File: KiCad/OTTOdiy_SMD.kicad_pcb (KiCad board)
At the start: 4 copper layers, 297 x 91 mm, 421 parts, among them CN201 1x4 MALE Molex PicoBlade, CN202 1x4 MALE Molex PicoBlade, J1 Conn_ARM_JTAG_SWD_10, J2 Conn_02x04, J201 Raspberry Pi Connector, J202 Conn_02x04, J203 Conn_02x05, J204 Conn_02x05, J205 Conn_02x04, J206 Conn_02x06, J207 Conn_02x03, Q1 AO4485, SW1 ALPS SKHH OR SKPF, SW10 ALPS SKHH OR SKPF, SW11 ALPS SKHH OR SKPF, SW12 ALPS SKHH OR SKPF, SW13 ALPS SKHH OR SKPF, SW14 ALPS SKHH OR SKPF, SW15 ALPS SKHH OR SKPF, SW16 ALPS SKHH OR SKPF, SW17 ALPS SKHH OR SKPF, SW18 ALPS SKHH OR SKPF, SW19 ALPS SKHH OR SKPF, SW2 ALPS SKHH OR SKPF, SW20 ALPS SKHH OR SKPF, SW201 6x6x5mm, SW202 SW_DIP_x02, SW203 6x6x5.85mm (RA), SW21 ALPS SKHH OR SKPF, SW22 ALPS SKHH OR SKPF, SW23 ALPS SKHH OR SKPF, SW24 ALPS SKHH OR SKPF, SW25 ALPS SKHH OR SKPF, SW26 ALPS SKHH OR SKPF, SW27 6x6x13mm, SW28 6x6x13mm, SW29 6x6x13mm, SW3 ALPS SKHH OR SKPF, SW30 6x6x13mm, SW31 6x6x13mm, SW32 6x6x13mm, SW33 6x6x13mm, SW34 6x6x13mm, SW35 6x6x13mm, SW36 6x6x13mm, SW37 6x6x13mm, SW38 6x6x13mm, SW39 6x6x13mm, SW4 ALPS SKHH OR SKPF, SW40 6x6x13mm, SW41 6x6x13mm, SW42 6x6x13mm, SW43 6x6x13mm, SW44 6x6x13mm, SW45 6x6x13mm, SW46 6x6x13mm, SW47 6x6x13mm, SW48 SW_DIP_x02, SW49 SW_SP3T (DP3T Parallel), SW5 ALPS SKHH OR SKPF, SW6 ALPS SKHH OR SKPF, SW7 ALPS SKHH OR SKPF, SW8 ALPS SKHH OR SKPF, SW9 ALPS SKHH OR SKPF, U1 SN74LV1T125_SOT-23_A, U2 TPS22918_SOT23-6_A, U202 STM32F407VGTx, U204 USB6B1, U205 SN74HC14, U206 H11L1S, U207 WM8731, U208 TPS79533, U3 LTC3112_TSSOP20_A, U4 TLV62568_SOT-23-5_A, U5 TPS22918_SOT23-6_A, Y201 8MHz, Y202 32.768kHz, Y203 12.288MHz

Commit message: more power supply routing and stm32 placement
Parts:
- moved C222 90.1 mm to (62.9, 52.5)
- moved C226 90.1 mm to (58.9, 58.5)
- moved C53 90.1 mm to (62.9, 49.5)
- moved C58 90.1 mm to (62.9, 46.5)
- moved C68 90.1 mm to (89.9, 36.3)
- moved R203 90.1 mm to (90.9, 45.0)
- moved R206 90.1 mm to (62.9, 55.5)
- moved R207 90.1 mm to (62.9, 58.5)
- moved SW202 90.1 mm to (83.6, 45.0)
- moved U206 90.1 mm to (83.6, 36.3)
- moved C211 84.2 mm to (56.6, 87.1)
- moved C221 84.2 mm to (56.6, 82.1)
- moved C50 84.2 mm to (53.6, 82.1)
- moved C54 84.2 mm to (65.6, 82.1)
- moved R204 84.2 mm to (59.6, 82.1)
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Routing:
- net GND: track 66.2 -> 231.8 mm, vias 37 -> 38
- net +3V3_MCU: track 35.5 -> 3.02 mm
- net +3V3A_MCU: track 17.1 -> 0.00 mm
- net /MCU/USBD_N: track 20.8 -> 6.91 mm
- net /MCU/USBD_P: track 20.1 -> 6.73 mm
- net /MCU/OSC_OUT: track 27.5 -> 14.2 mm, vias 0 -> 1
- net /MCU/OSC_IN: track 23.3 -> 14.3 mm, vias 0 -> 1
- net Net-(D9-Pad2): track 0.00 -> 8.30 mm
- net Net-(D8-Pad2): track 0.00 -> 8.30 mm
- net Net-(D7-Pad2): track 0.00 -> 8.30 mm
- net Net-(D6-Pad2): track 0.00 -> 8.30 mm
- net Net-(D23-Pad2): track 0.00 -> 8.30 mm
- net Net-(D22-Pad2): track 0.00 -> 8.30 mm
- net Net-(D21-Pad2): track 0.00 -> 8.30 mm
- net Net-(D20-Pad2): track 0.00 -> 8.30 mm
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- added copper zone on B.Cu, net +5V_LEDS

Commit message: routed mcu decoupling
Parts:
- removed C223: 1uF, Capacitor_SMD:C_0805_2012Metric_Pad1.15x1.40mm_HandSolder
- removed C56: 100nF, Capacitor_SMD:C_0805_2012Metric_Pad1.15x1.40mm_HandSolder
- BT201: moved to F.Cu
- C96, C97, FB1: moved to B.Cu
- moved FB1 108.9 mm to (105.0, 158.3), turned to 180 degrees
- moved BT201 99.9 mm to (110.5, 129.0)
- moved C96 98.4 mm to (105.0, 143.1)
- moved C53 96.1 mm to (81.0, 143.9)
- moved C97 93.8 mm to (105.0, 145.0)
- moved C51 90.6 mm to (98.0, 162.1), turned to 270 degrees
- moved C50 87.3 mm to (105.0, 152.6), turned to 0 degrees
- moved C52 84.9 mm to (87.0, 162.1), turned to 270 degrees
- moved C49 84.7 mm to (105.0, 146.9)
- moved C218 76.9 mm to (105.0, 141.2)
- moved C55 75.4 mm to (105.0, 154.5)
- moved C219 74.4 mm to (105.0, 156.4)
- moved C211 67.4 mm to (100.9, 137.9), turned to 90 degrees
- moved C54 65.0 mm to (99.0, 137.9), turned to 90 degrees
- moved C205 24.0 mm to (105.0, 150.7)
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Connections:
- Y202 pad 1: /MCU/OSC32_OUT -> /MCU/OSC32_IN
- Y202 pad 2: /MCU/OSC32_IN -> GND
- Y202 pad 3: (no net) -> GND
- Y202 pad 4: (no net) -> /MCU/OSC32_OUT
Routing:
- net Net-(LED18-Pad1): track 0.00 -> 37.7 mm
- net GND: track 231.8 -> 257.6 mm, vias 38 -> 52
- net +3V3_MCU: track 3.02 -> 28.6 mm, vias 5 -> 12
- net /MCU/VBAT: track 0.00 -> 21.3 mm, vias 0 -> 1
- net Net-(LED19-Pad1): track 0.00 -> 14.2 mm
- net Net-(LED17-Pad1): track 0.00 -> 14.2 mm
- net +3V3A_MCU: track 0.00 -> 10.1 mm
- net /MCU/OSC32_IN: track 2.25 -> 12.2 mm
- net /MCU/OSC32_OUT: track 2.25 -> 10.8 mm
- net Net-(LED21-Pad1): track 42.9 -> 38.0 mm
- net Net-(LED23-Pad1): track 36.1 -> 32.2 mm
- net +5V_LEDS: track 167.5 -> 169.5 mm, vias 6 -> 5
- net Net-(LED4-Pad1): track 20.5 -> 18.8 mm
- net /MCU/OSC_OUT: track 14.2 -> 15.3 mm
- net /MCU/OSC_IN: track 14.3 -> 15.3 mm
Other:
- net class Default: clearance 0.254 -> 0.2032
- rule trace_clearance: 0.254 -> 0.2032

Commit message: fix peripheral connections and route more critical components
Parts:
- added C56: 100nF, Capacitor_SMD:C_0805_2012Metric_Pad1.15x1.40mm_HandSolder, B.Cu at (105.0, 162.1)
- added R29: 10k, Resistor_SMD:R_0805_2012Metric_Pad1.15x1.40mm_HandSolder, B.Cu at (105.0, 164.0)
- added R30: 10k, Resistor_SMD:R_0805_2012Metric_Pad1.15x1.40mm_HandSolder, B.Cu at (105.0, 165.9)
- added TP1: TestPoint, TestPoint:TestPoint_Keystone_5000-5004_Miniature, F.Cu at (181.4, 83.8)
- C57, R5, R8: moved to B.Cu
- PHOTO201: value ALS-PDIC243-3B -> VAL**
- USB201: value USB_B -> VAL**
- moved R28 205.1 mm to (81.0, 151.9), turned to 180 degrees
- moved D57 201.1 mm to (81.0, 153.8), turned to 180 degrees
- moved R5 138.2 mm to (61.1, 134.7), turned to 90 degrees
- moved R8 131.6 mm to (59.2, 134.7), turned to 90 degrees
- moved C57 102.2 mm to (105.0, 160.2), turned to 180 degrees
- moved R206 94.3 mm to (81.0, 148.1)
- moved R207 93.2 mm to (81.0, 150.0)
- moved C222 93.0 mm to (81.9, 143.6), turned to 90 degrees
- moved C221 85.7 mm to (87.5, 162.1)
- moved J1 42.3 mm to (103.0, 122.6)
- moved C53 3.70 mm to (82.8, 140.8)
- moved BT201 1.60 mm to (112.1, 129.0)
- moved U204 1.50 mm to (79.5, 125.0)
- moved C52 1.45 mm to (85.5, 162.1)
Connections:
- net /MCU/PERIPHERALS/USBD_N_CON renamed /MCU/PERIPHERALS/USBCON_N
- net /MCU/PERIPHERALS/USBD_P_CON renamed /MCU/PERIPHERALS/USBCON_P
- R28 pad 1: Net-(R28-Pad1) -> /MCU/STATUS_LED
- SW48 pad 1: +5V_REG -> +3V3_MCU
- SW48 pad 2: +5V_REG -> +3V3_MCU
- U202 pad 16: /MCU/DC_IN_DIV_5 -> (no net)
- U202 pad 17: /MCU/5V_REG_IOUT -> (no net)
- U202 pad 18: /MCU/BRIGHTNESS -> (no net)
- U202 pad 23: PWR_BUTTON -> /MCU/DC_IN_DIV_5
- U202 pad 24: (no net) -> /MCU/BRIGHTNESS
- U202 pad 25: (no net) -> /MCU/3V3_RASPI_DIV_2
- U202 pad 26: (no net) -> /MCU/5V_REG_IOUT
- U202 pad 33: /MCU/GATE_IO_1 -> /MCU/EXP_GPIO_1_ADC
- U202 pad 34: /MCU/GATE_IO_2 -> /MCU/EXP_GPIO_2_ADC
- U202 pad 35: /MCU/EXP_GPIO_1_ADC -> /MCU/GATE_IO_1
- U202 pad 36: /MCU/EXP_GPIO_2_ADC -> /MCU/GATE_IO_2
- U202 pad 38: /MCU/EXP_GPIO_3_PWM -> (no net)
- U202 pad 39: /MCU/EXP_GPIO_4_PWM -> (no net)
- U202 pad 40: /MCU/EXP_GPIO_5_PWM -> /MCU/EXP_GPIO_3_PWM
- U202 pad 41: /MCU/EXP_GPIO_6_PWM -> (no net)
- U202 pad 42: (no net) -> /MCU/EXP_GPIO_4_PWM
- U202 pad 44: Net-(R28-Pad1) -> /MCU/EXP_GPIO_5_PWM
- U202 pad 45: /MCU/5V_PWM_SYNC -> /MCU/EXP_GPIO_6_PWM
- U202 pad 62: (no net) -> /PWM1_GPIO13_RASPI
- U202 pad 63: /GPIO0_RASPI -> /MCU/STATUS_LED
- U202 pad 64: /GPIO1_RASPI -> /MCU/5V_PWM_SYNC
- U202 pad 65: /PWM1_GPIO13_RASPI -> /MCU/MCU_PC8
- U202 pad 81: Net-(R25-Pad1) -> PWR_BUTTON
- U202 pad 82: (no net) -> Net-(R25-Pad1)
- U202 pad 92: (no net) -> /GPIO0_RASPI
- U202 pad 93: (no net) -> /GPIO1_RASPI
- U202 pad 97: (no net) -> /MCU/LED_PWR_EN
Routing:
- net /MCU/+5V_USB: track 55.8 -> 81.9 mm, vias 0 -> 2
- net /MCU/USBD_N: track 6.91 -> 24.3 mm
- net /MCU/USBD_P: track 6.73 -> 23.5 mm
- net /MCU/DC_IN: track 27.7 -> 38.5 mm, vias 8 -> 9
- net /MCU/DC_IN_DIV_5: track 0.00 -> 9.75 mm
- net GND: track 257.6 -> 266.7 mm, vias 52 -> 53
- net +3V3_MCU: track 28.6 -> 32.8 mm
- net /MCU/I2C2_SDA: track 0.00 -> 3.97 mm
- net /MCU/3V3_RASPI_DIV_2: track 0.00 -> 3.80 mm
- net Net-(C222-Pad1): track 0.00 -> 3.60 mm
- net /MCU/I2C2_SCL: track 0.00 -> 3.39 mm
- net Net-(C221-Pad1): track 0.00 -> 3.37 mm
- net /MCU/PERIPHERALS/USBCON_P: track 9.13 -> 6.95 mm
- net /MCU/PERIPHERALS/USBCON_N: track 6.27 -> 4.76 mm
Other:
- net class Default: clearance 0.2032 -> 0.2
- net class USB: clearance 0.18 -> 0.2; trace_width 0.25 -> 0.261112
- rule trace_clearance: 0.2032 -> 0.2
- rule trace_min: 0.127 -> 0.2032

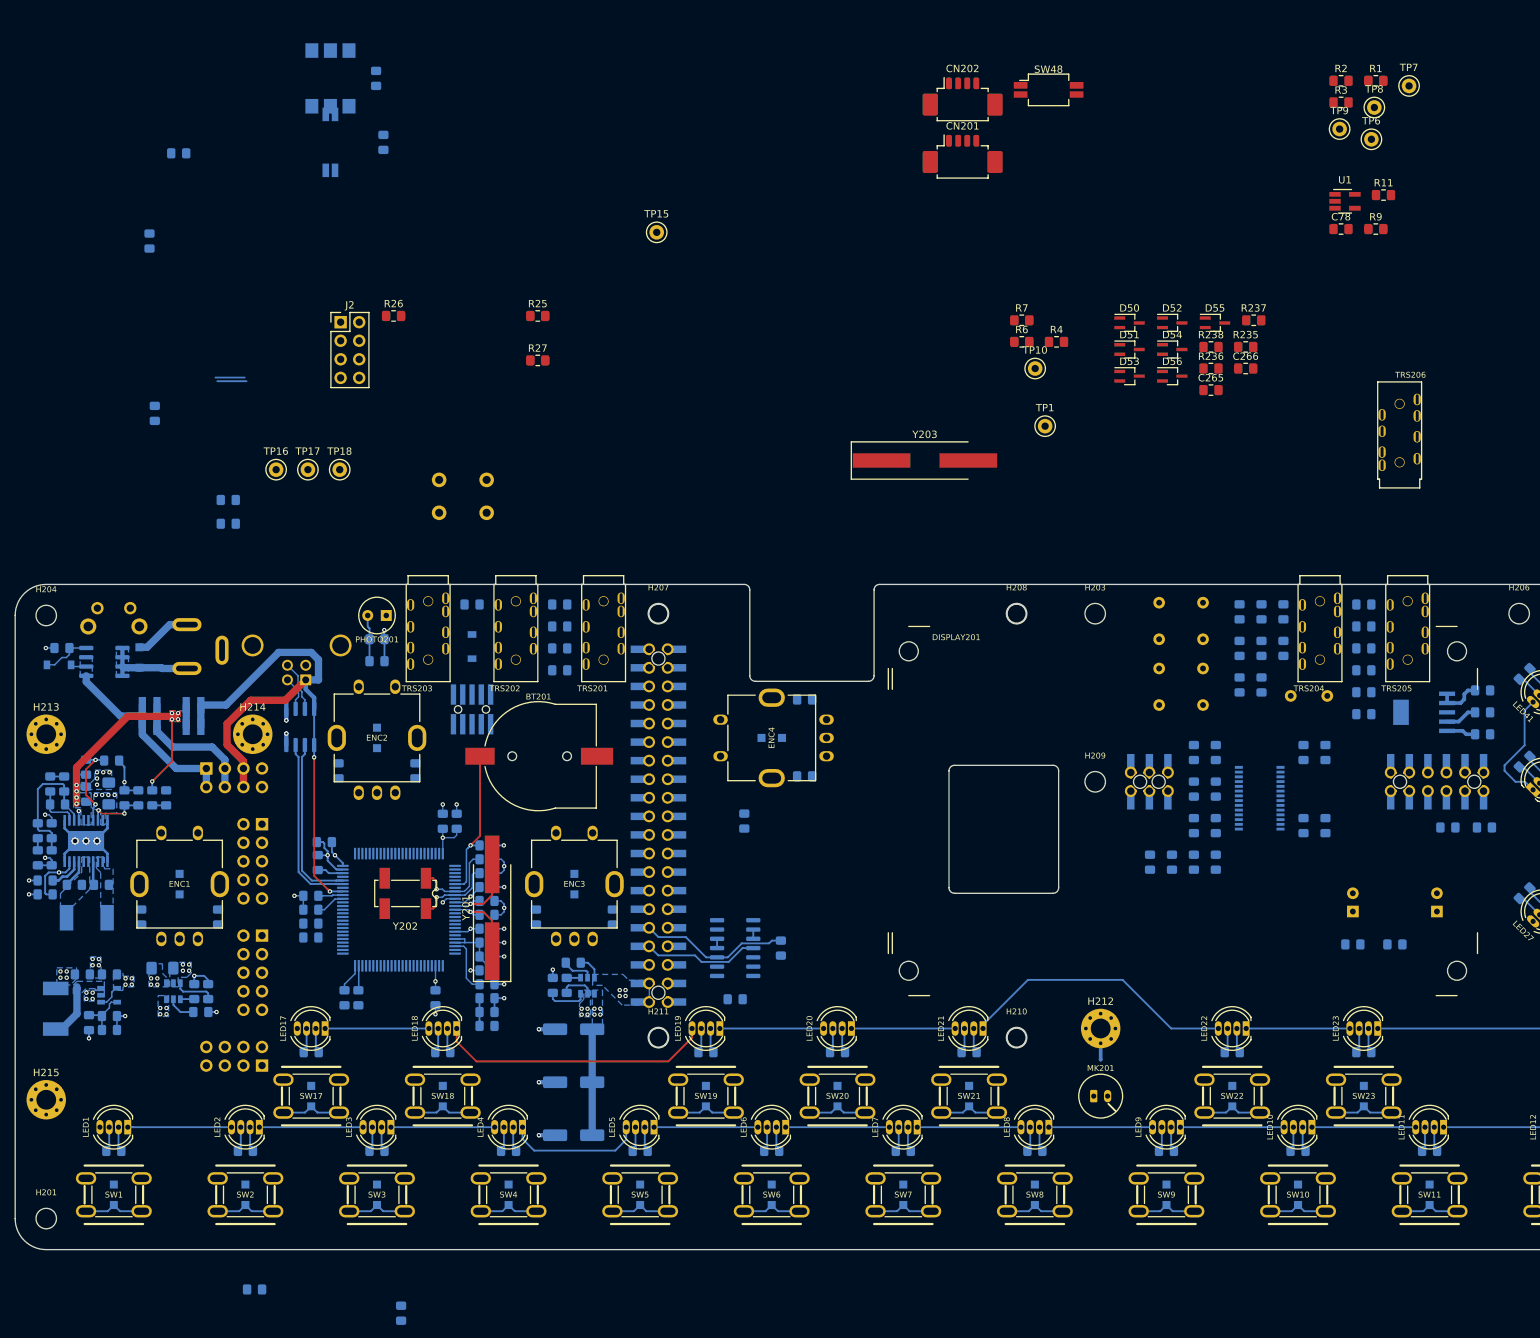
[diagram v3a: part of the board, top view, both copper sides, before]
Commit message: routed audio
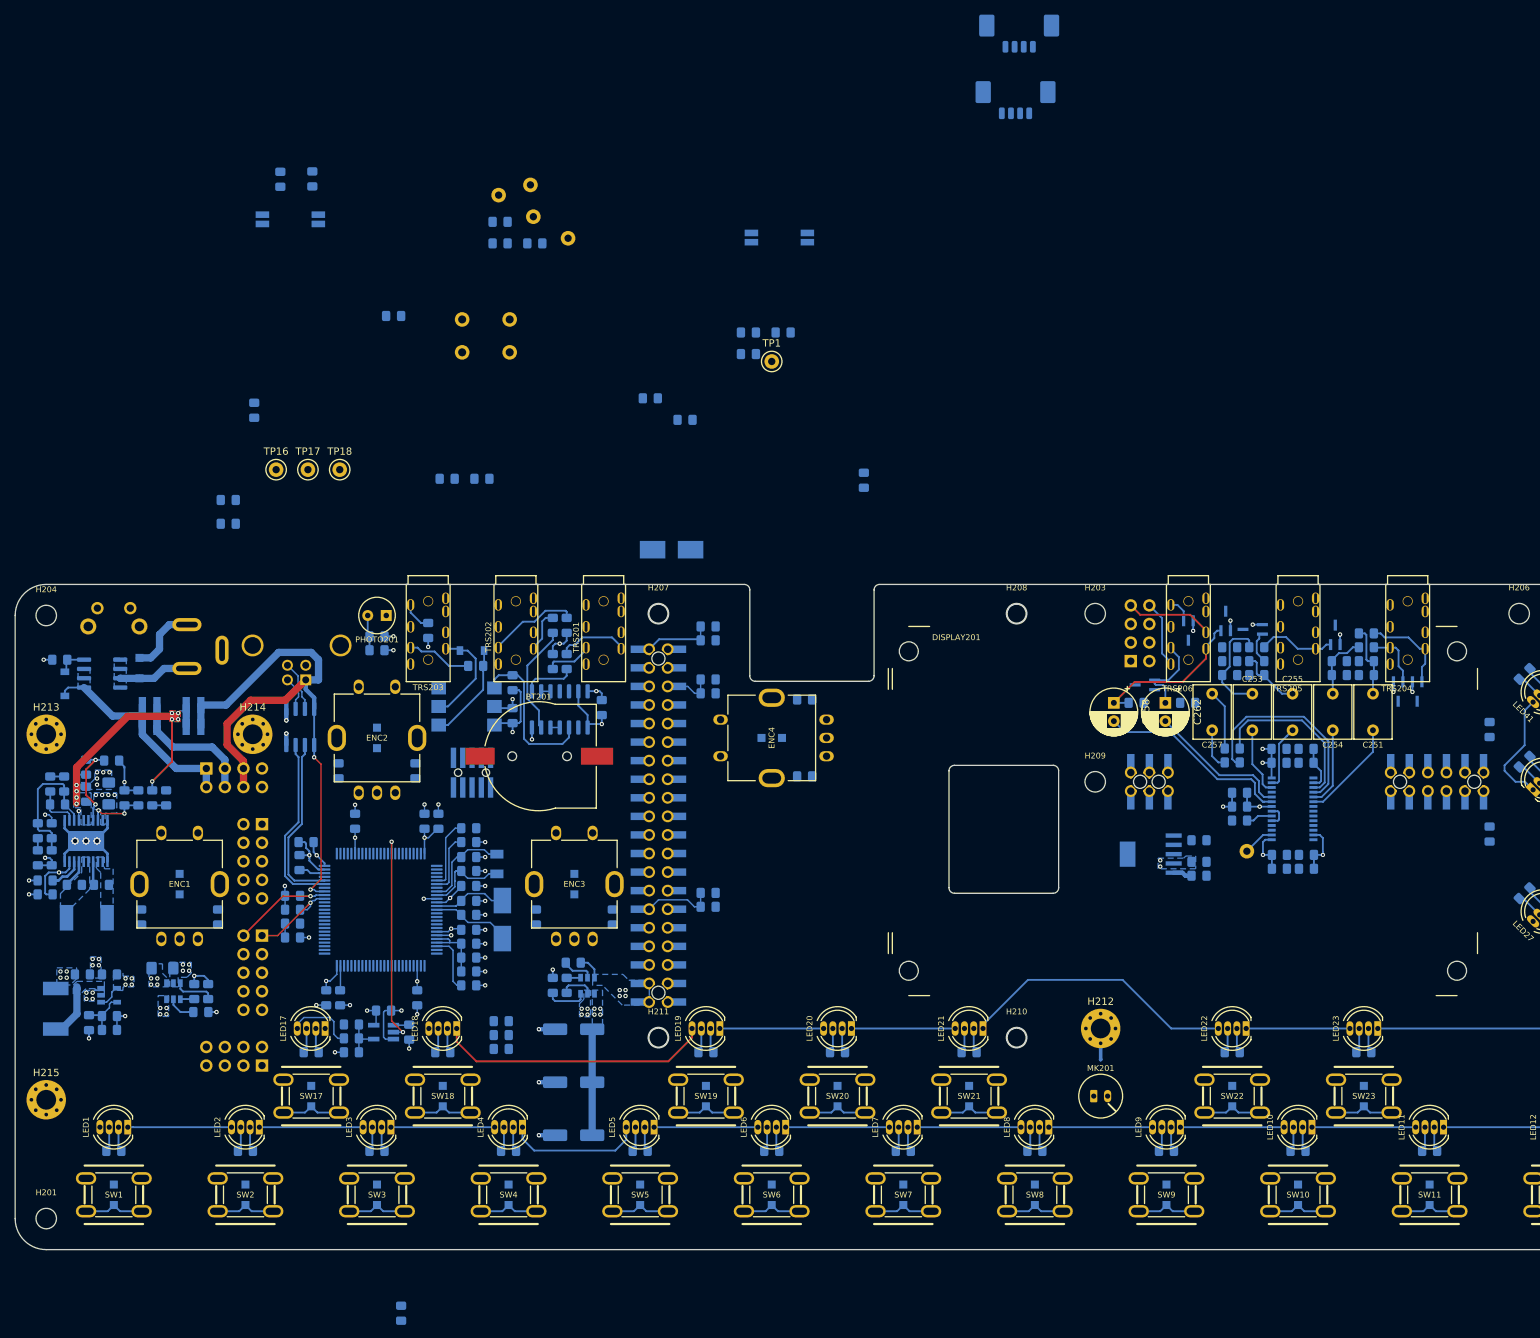
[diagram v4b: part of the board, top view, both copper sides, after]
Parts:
- removed R25: 10k, Resistor_SMD:R_0805_2012Metric_Pad1.15x1.40mm_HandSolder
- removed TP10: TestPoint, TestPoint:TestPoint_Keystone_5000-5004_Miniature
- added C98: 100nF, Capacitor_SMD:C_0805_2012Metric_Pad1.15x1.40mm_HandSolder, B.Cu at (97.0, 111.8)
- added R31: 10k, Resistor_SMD:R_0805_2012Metric_Pad1.15x1.40mm_HandSolder, B.Cu at (99.6, 91.0)
- added R32: 10k, Resistor_SMD:R_0805_2012Metric_Pad1.15x1.40mm_HandSolder, B.Cu at (104.3, 91.0)
- C251, C253, C254, C255, C257, C258, C262: moved to F.Cu
- C265, C266, C78, CN201, CN202, D50, D51, D52, D53, D54, D55, D56, J2, R1, R11, R2, R235, R236, R237, R238, R26, R27, R3, R4, R6, R7, R9, SW48, TP15, TP6, TP7, TP8, TP9, U1: moved to B.Cu
- PHOTO201: value VAL** -> ALS-PDIC243-3B
- USB201: value VAL** -> USB_B
- Y201: value 8MHz -> 25MHz; footprint Crystal:Crystal_SMD_HC49-SD_HandSoldering -> Crystal:Crystal_SMD_5032-2Pin_5.0x3.2mm_HandSoldering; moved to B.Cu
- Y202: footprint Crystal:Crystal_SMD_SeikoEpson_MC306-4Pin_8.0x3.2mm_HandSoldering -> OTTO_Footprints_Lib:Crystal_SMD_3215-2Pin_3.2x1.5mm_HandSoldering; moved to B.Cu
- Y203: footprint Crystal:Crystal_SMD_HC49-SD_HandSoldering -> Crystal:Crystal_SMD_5032-2Pin_5.0x3.2mm_HandSoldering; moved to B.Cu
- moved R11 183.5 mm to (86.5, 169.5), turned to 180 degrees
- moved U1 173.8 mm to (90.9, 166.8), turned to 180 degrees
- moved R9 171.9 mm to (94.4, 166.8), turned to 90 degrees
- moved C78 169.1 mm to (90.9, 163.8)
- moved R237 127.9 mm to (102.5, 138.8), turned to 180 degrees
- moved J2 117.6 mm to (193.1, 116.0)
- moved R1 117.2 mm to (111.6, 58.8)
- moved R2 117.2 mm to (106.8, 58.8)
- moved TP15 117.0 mm to (209.0, 142.0)
- moved TP7 116.9 mm to (116.1, 58.1)
- moved R3 116.2 mm to (106.8, 55.9)
- moved TP8 116.0 mm to (111.4, 55.2)
- moved TP9 115.4 mm to (106.6, 52.2)
- moved TP6 115.2 mm to (111.0, 50.8)
- moved R235 104.8 mm to (135.3, 147.7)
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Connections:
- D54 pad 1: GND -> /AUDIO/MIC_IN
- D54 pad 2: /AUDIO/MIC_IN -> GND
- D55 pad 1: GND -> /AUDIO/HP_OUT_R
- D55 pad 2: /AUDIO/HP_OUT_R -> GND
- R10 pad 1: /MCU/LED_PWR_EN -> Net-(R10-Pad1)
- R16 pad 1: PI_PWR_EN -> Net-(R16-Pad1)
- SW48 pad 3: /MCU/LED_PWR_EN -> Net-(R10-Pad1)
- SW48 pad 4: PI_PWR_EN -> Net-(R16-Pad1)
- TRS201 pad R1: Net-(R212-Pad2) -> Net-(R213-Pad2)
- TRS201 pad T: Net-(R213-Pad2) -> Net-(R212-Pad2)
- TRS202 pad R1: Net-(R214-Pad2) -> Net-(R215-Pad2)
- TRS202 pad T: Net-(R215-Pad2) -> Net-(R214-Pad2)
- TRS203 pad S: (no net) -> Net-(C98-Pad2)
- U2 pad 3: /MCU/LED_PWR_EN -> Net-(R10-Pad1)
- U202 pad 15: (no net) -> /MCU/ROW_5
- U202 pad 16: (no net) -> /MCU/ROW_6
- U202 pad 17: (no net) -> /MCU/ROW_7
- U202 pad 18: (no net) -> /MCU/ROW_8
- U202 pad 38: (no net) -> /MCU/COL_3
- U202 pad 39: (no net) -> /MCU/COL_4
- U202 pad 41: (no net) -> /MCU/COL_5
- U202 pad 43: (no net) -> /MCU/COL_6
- U202 pad 46: (no net) -> /MCU/COL_7
- U202 pad 51: (no net) -> /MCU/ROW_1
- U202 pad 52: (no net) -> /MCU/ROW_2
- U202 pad 53: (no net) -> /MCU/ROW_3
- U202 pad 54: (no net) -> /MCU/ROW_4
- U202 pad 55: (no net) -> /MCU/ENC_A_3
- U202 pad 56: (no net) -> /MCU/ENC_B_3
- U202 pad 57: (no net) -> /MCU/ENC_A_4
- U202 pad 58: (no net) -> /MCU/ENC_B_4
- U202 pad 69: (no net) -> /MCU/LED_PWR_EN
- U202 pad 7: /MCU/TAMPER_RTC -> (no net)
- U202 pad 82: Net-(R25-Pad1) -> PI_PWR_EN
- U202 pad 83: (no net) -> /MCU/ENC_A_1
- U202 pad 84: (no net) -> /MCU/ENC_B_1
- U202 pad 85: (no net) -> /MCU/ENC_A_2
- U202 pad 88: (no net) -> /MCU/ENC_B_2
- U202 pad 97: /MCU/LED_PWR_EN -> /MCU/COL_1
- U202 pad 98: (no net) -> /MCU/COL_2
- U5 pad 3: PI_PWR_EN -> Net-(R16-Pad1)
- Y202 pad 1: /MCU/OSC32_IN -> /MCU/OSC32_OUT
- Y202 pad 2: GND -> /MCU/OSC32_IN
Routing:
- net GND: track 266.7 -> 301.2 mm, vias 53 -> 72
- net +3V3_RASPI: track 0.00 -> 30.7 mm, vias 0 -> 5
- net /MCU/SPI_MOSI_MCU: track 0.00 -> 29.6 mm, vias 0 -> 2
- net Net-(R227-Pad1): track 0.00 -> 28.8 mm
- net Net-(C258-Pad2): track 0.00 -> 27.0 mm
- net Net-(R226-Pad1): track 0.00 -> 23.3 mm
- net /AUDIO/HP_OUT_L: track 0.00 -> 22.1 mm
- net Net-(C262-Pad2): track 0.00 -> 19.7 mm
- net MIDI_OUT: track 15.9 -> 0.00 mm
- net Net-(R214-Pad1): track 0.00 -> 15.2 mm
- net Net-(C253-Pad1): track 0.00 -> 14.6 mm
- net Net-(LED17-Pad1): track 14.2 -> 0.00 mm
- net Net-(D206-Pad2): track 0.00 -> 14.0 mm
- net Net-(C251-Pad1): track 0.00 -> 13.9 mm
- net Net-(D206-Pad1): track 0.00 -> 13.5 mm
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- added copper zone on B.Cu, net +3V3_ANALOG
